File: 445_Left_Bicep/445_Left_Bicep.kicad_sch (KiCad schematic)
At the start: 17 parts, among them J1 69167-107HLF, J2 SM02B-SRSS-TB_LF__SN_, J3 87583-2010RPLF, J4 69167-107HLF, U1 LSM6DSMTR, U2 ESP32-S3-WROOM-1-N16R8, U3 TS3A5018D, U4 LP2950CZ-3.3_LFT3, U5 TS3A5018D

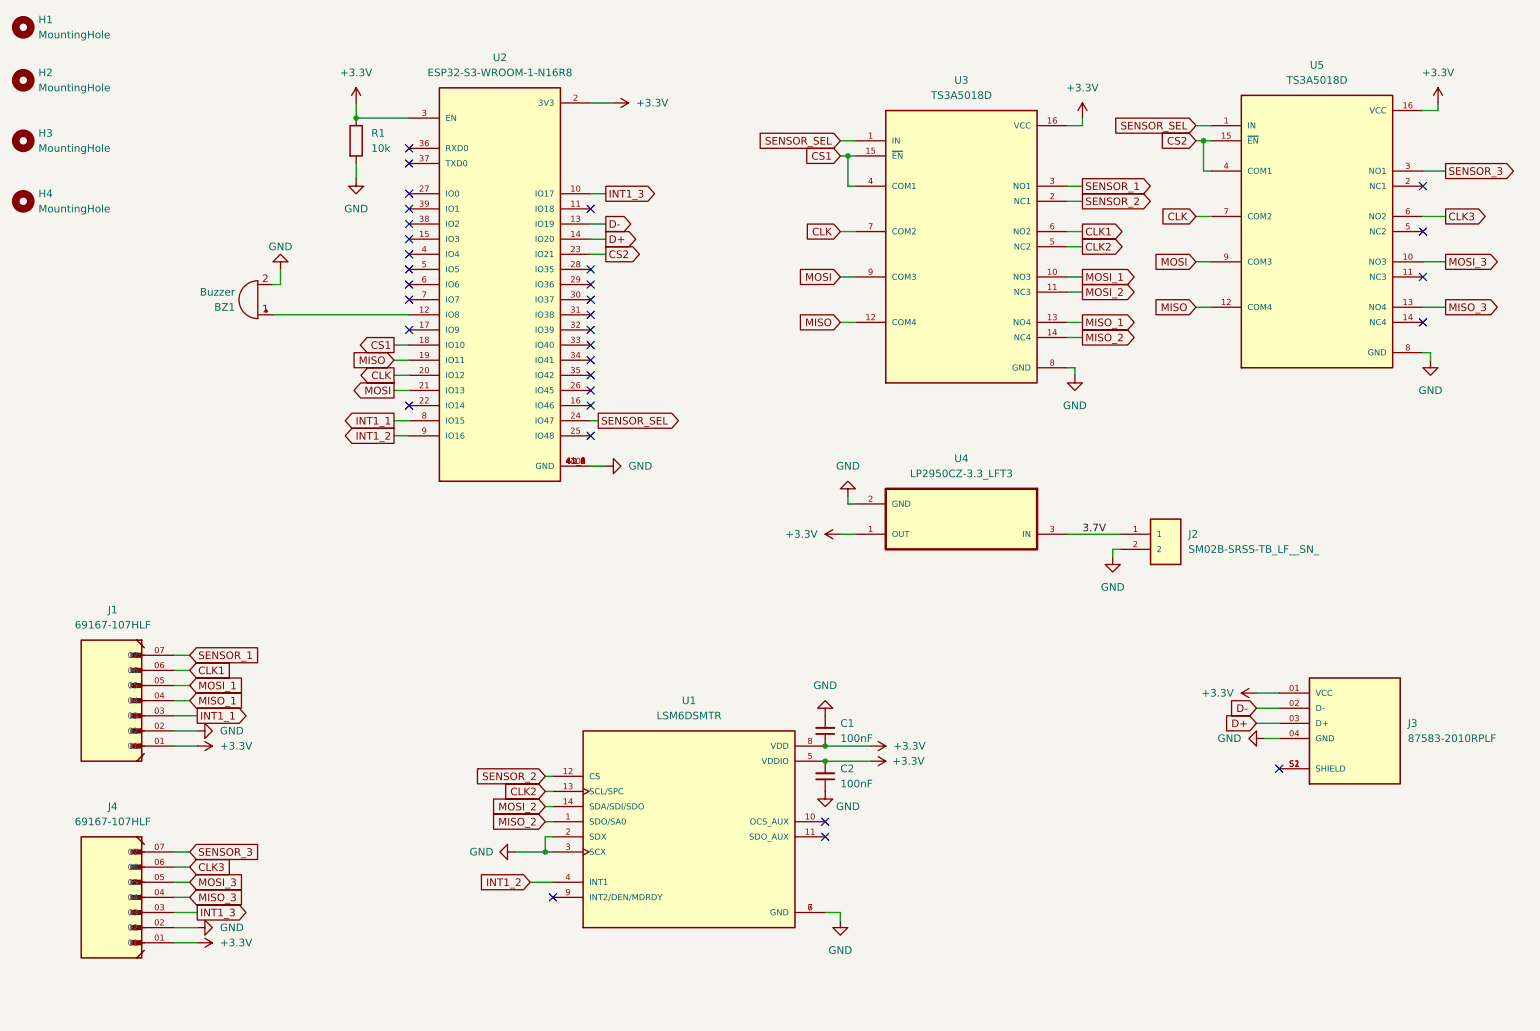
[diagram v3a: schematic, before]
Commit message: adding buzzer
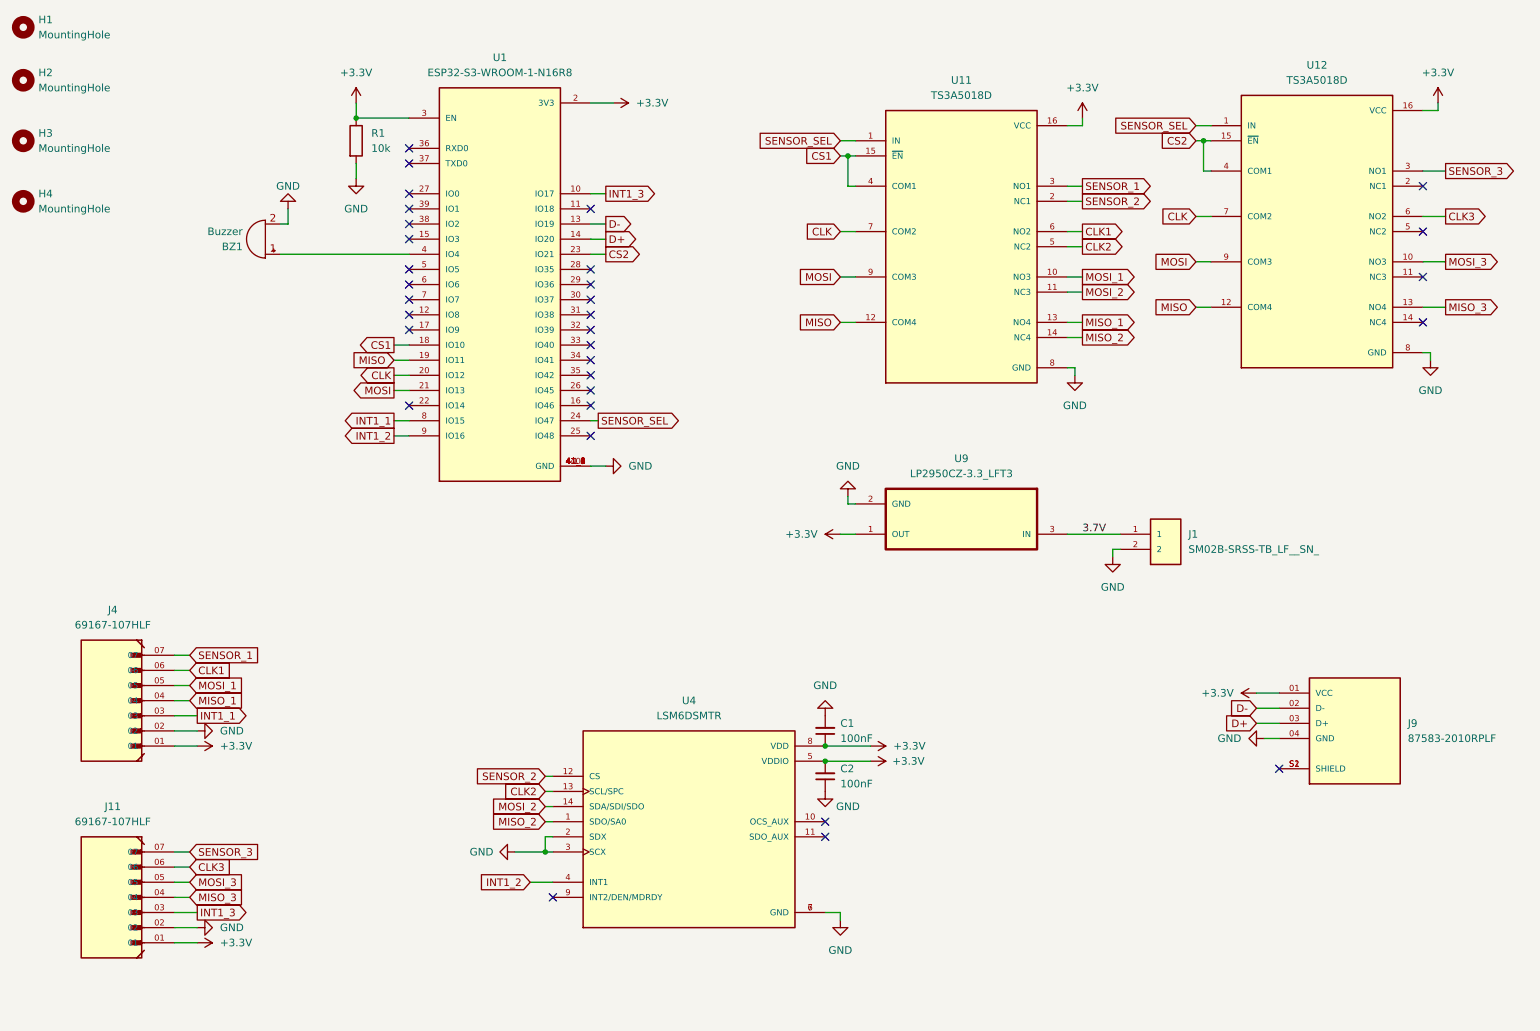
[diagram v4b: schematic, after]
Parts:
- renumbered J2 to J1, J4 to J11, J1 to J4, J3 to J9, U2 to U1, U3 to U11, U5 to U12, U1 to U4, U4 to U9
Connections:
- net at BZ1.1 (+): now also U1.4 (IO4); no longer U1.12 (IO8)
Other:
- moved on the sheet: BZ1
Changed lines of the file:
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@@
   (junction (at 156.21 144.78) (diameter 0) (color 0 0 0 0)
   )
-  (no_connect (at 86.36 59.69))
   (no_connect (at 116.84 90.17))
   (no_connect (at 116.84 74.93))
@@
   (no_connect (at 156.21 157.48))
   (no_connect (at 232.41 146.05))
+  (no_connect (at 86.36 69.85))
   (no_connect (at 256.54 63.5))
   (no_connect (at 86.36 67.31))
@@
     (stroke (width 0) (type default))
   )
-  (wire (pts (xy 63.5 69.85) (xy 86.36 69.85))
-    (stroke (width 0) (type default))
-  )
   (wire (pts (xy 219.71 45.72) (xy 220.98 45.72))
     (stroke (width 0) (type default))
@@
     (stroke (width 0) (type default))
   )
-  (wire (pts (xy 64.77 64.77) (xy 63.5 64.77))
+  (wire (pts (xy 66.04 54.61) (xy 64.77 54.61))
     (stroke (width 0) (type default))
   )
@@
     (stroke (width 0) (type default))
   )
-  (wire (pts (xy 64.77 62.23) (xy 64.77 64.77))
+  (wire (pts (xy 64.77 59.69) (xy 86.36 59.69))
+    (stroke (width 0) (type default))
+  )
+  (wire (pts (xy 66.04 52.07) (xy 66.04 54.61))
     (stroke (width 0) (type default))
   )
@@
   (symbol (lib_id "LP2950CZ-3.3_LFT3:LP2950CZ-3.3_LFT3") (at 179.07 104.14 180) (unit 1)
     (in_bom yes) (on_board yes) (dnp no) (fields_autoplaced)
-    (property "Reference" "U4" (at 179.07 93.98 0)
+    (property "Reference" "U9" (at 179.07 93.98 0)
       (effects (font (size 1.27 1.27)))
     )
@@
       (project "445_Left_Bicep"
         (path "/5276b365-6d0c-4da8-be37-f3b7813500d7"
-          (reference "U4") (unit 1)
-        )
-      )
-    )
-  )
-  (symbol (lib_id "Device:Buzzer") (at 60.96 67.31 180) (unit 1)
-    (in_bom yes) (on_board yes) (dnp no) (fields_autoplaced)
-    (property "Reference" "BZ1" (at 57.15 68.58 0)
-      (effects (font (size 1.27 1.27)) (justify left))
-    )
-    (property "Value" "Buzzer" (at 57.15 66.04 0)
-      (effects (font (size 1.27 1.27)) (justify left))
-    )
-    (property "Footprint" "ECE 445 Footprints:AC-903-D-1P" (at 61.595 69.85 90)
-      (effects (font (size 1.27 1.27)) hide)
-    )
-    (property "Datasheet" "~" (at 61.595 69.85 90)
+          (reference "U9") (unit 1)
+        )
+      )
+    )
+  )
+  (symbol (lib_id "Device:Buzzer") (at 62.23 57.15 180) (unit 1)
+    (in_bom yes) (on_board yes) (dnp no) (fields_autoplaced)
+    (property "Reference" "BZ1" (at 58.42 58.42 0)
+      (effects (font (size 1.27 1.27)) (justify left))
+    )
+    (property "Value" "Buzzer" (at 58.42 55.88 0)
+      (effects (font (size 1.27 1.27)) (justify left))
+    )
+    (property "Footprint" "ECE 445 Footprints:AC-903-D-1P" (at 62.865 59.69 90)
+      (effects (font (size 1.27 1.27)) hide)
+    )
+    (property "Datasheet" "~" (at 62.865 59.69 90)
       (effects (font (size 1.27 1.27)) hide)
     )
@@
   (symbol (lib_id "SM02B-SRSS-TB_LF__SN_:SM02B-SRSS-TB_LF__SN_") (at 205.74 111.76 0) (unit 1)
     (in_bom yes) (on_board yes) (dnp no) (fields_autoplaced)
-    (property "Reference" "J2" (at 217.17 106.68 0)
+    (property "Reference" "J1" (at 217.17 106.68 0)
       (effects (font (size 1.27 1.27)) (justify left))
     )
@@
       (project "445_Left_Bicep"
         (path "/5276b365-6d0c-4da8-be37-f3b7813500d7"
-          (reference "J2") (unit 1)
+          (reference "J1") (unit 1)
         )
       )
@@
   (symbol (lib_id "LSM6DSMTR:LSM6DSMTR") (at 133.35 154.94 0) (unit 1)
     (in_bom yes) (on_board yes) (dnp no) (fields_autoplaced)
-    (property "Reference" "U1" (at 133.35 134.62 0)
+    (property "Reference" "U4" (at 133.35 134.62 0)
       (effects (font (size 1.27 1.27)))
     )
@@
       (project "445_Left_Bicep"
         (path "/5276b365-6d0c-4da8-be37-f3b7813500d7"
-          (reference "U1") (unit 1)
+          (reference "U4") (unit 1)
         )
       )
@@
   (symbol (lib_id "TS3A5018D:TS3A5018D") (at 179.07 58.42 0) (unit 1)
     (in_bom yes) (on_board yes) (dnp no) (fields_autoplaced)
-    (property "Reference" "U3" (at 179.07 30.48 0)
+    (property "Reference" "U11" (at 179.07 30.48 0)
       (effects (font (size 1.27 1.27)))
     )
@@
       (project "445_Left_Bicep"
         (path "/5276b365-6d0c-4da8-be37-f3b7813500d7"
-          (reference "U3") (unit 1)
-        )
-      )
-    )
-  )
-  (symbol (lib_id "power:GND") (at 64.77 62.23 180) (unit 1)
+          (reference "U11") (unit 1)
+        )
+      )
+    )
+  )
+  (symbol (lib_id "power:GND") (at 66.04 52.07 180) (unit 1)
     (in_bom yes) (on_board yes) (dnp no)
-    (property "Reference" "#PWR05" (at 64.77 55.88 0)
-      (effects (font (size 1.27 1.27)) hide)
-    )
-    (property "Value" "GND" (at 64.77 58.42 0)
-      (effects (font (size 1.27 1.27)))
-    )
-    (property "Footprint" "" (at 64.77 62.23 0)
-      (effects (font (size 1.27 1.27)) hide)
-    )
-    (property "Datasheet" "" (at 64.77 62.23 0)
+    (property "Reference" "#PWR05" (at 66.04 45.72 0)
+      (effects (font (size 1.27 1.27)) hide)
+    )
+    (property "Value" "GND" (at 66.04 48.26 0)
+      (effects (font (size 1.27 1.27)))
+    )
+    (property "Footprint" "" (at 66.04 52.07 0)
+      (effects (font (size 1.27 1.27)) hide)
+    )
+    (property "Datasheet" "" (at 66.04 52.07 0)
       (effects (font (size 1.27 1.27)) hide)
     )
@@
   (symbol (lib_id "69167-107HLF:69167-107HLF") (at 36.83 167.64 180) (unit 1)
     (in_bom yes) (on_board yes) (dnp no) (fields_autoplaced)
-    (property "Reference" "J4" (at 36.6135 152.4 0)
+    (property "Reference" "J11" (at 36.6135 152.4 0)
       (effects (font (size 1.27 1.27)))
     )
@@
       (project "445_Left_Bicep"
         (path "/5276b365-6d0c-4da8-be37-f3b7813500d7"
-          (reference "J4") (unit 1)
+          (reference "J11") (unit 1)
         )
       )
@@
   (symbol (lib_id "87583-2010RPLF:87583-2010RPLF") (at 245.11 140.97 0) (unit 1)
     (in_bom yes) (on_board yes) (dnp no) (fields_autoplaced)
-    (property "Reference" "J3" (at 254 138.43 0)
+    (property "Reference" "J9" (at 254 138.43 0)
       (effects (font (size 1.27 1.27)) (justify left))
     )
@@
       (project "445_Left_Bicep"
         (path "/5276b365-6d0c-4da8-be37-f3b7813500d7"
-          (reference "J3") (unit 1)
+          (reference "J9") (unit 1)
         )
       )
@@
   (symbol (lib_id "TS3A5018D:TS3A5018D") (at 238.76 55.88 0) (unit 1)
     (in_bom yes) (on_board yes) (dnp no) (fields_autoplaced)
-    (property "Reference" "U5" (at 238.76 27.94 0)
+    (property "Reference" "U12" (at 238.76 27.94 0)
       (effects (font (size 1.27 1.27)))
     )
@@
       (project "445_Left_Bicep"
         (path "/5276b365-6d0c-4da8-be37-f3b7813500d7"
-          (reference "U5") (unit 1)
+          (reference "U12") (unit 1)
         )
       )
@@
   (symbol (lib_id "ESP32-S3-WROOM-1-N16R8:ESP32-S3-WROOM-1-N16R8") (at 101.6 62.23 0) (unit 1)
     (in_bom yes) (on_board yes) (dnp no) (fields_autoplaced)
-    (property "Reference" "U2" (at 101.6 26.67 0)
+    (property "Reference" "U1" (at 101.6 26.67 0)
       (effects (font (size 1.27 1.27)))
     )
@@
       (project "445_Left_Bicep"
         (path "/5276b365-6d0c-4da8-be37-f3b7813500d7"
-          (reference "U2") (unit 1)
+          (reference "U1") (unit 1)
         )
       )
@@
   (symbol (lib_id "69167-107HLF:69167-107HLF") (at 36.83 134.62 180) (unit 1)
     (in_bom yes) (on_board yes) (dnp no) (fields_autoplaced)
-    (property "Reference" "J1" (at 36.6135 119.38 0)
+    (property "Reference" "J4" (at 36.6135 119.38 0)
       (effects (font (size 1.27 1.27)))
     )
@@
       (project "445_Left_Bicep"
         (path "/5276b365-6d0c-4da8-be37-f3b7813500d7"
-          (reference "J1") (unit 1)
-        )
-      )
+          (reference "J4") (unit 1)
+        )
+      )
